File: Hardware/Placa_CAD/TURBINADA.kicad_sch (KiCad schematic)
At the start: 49 parts, among them J1 TURBINA, J2 RESISTENCIAS, J3 BATERIA, J4 ICSP, Q1 IXTP44P15T, Q2 IXTP36P15P, Q3 FQN1N50C, Q4 FQN1N50C, U1 PIC16F18324-xSL, U2 ADP2302ARDZ-5.0

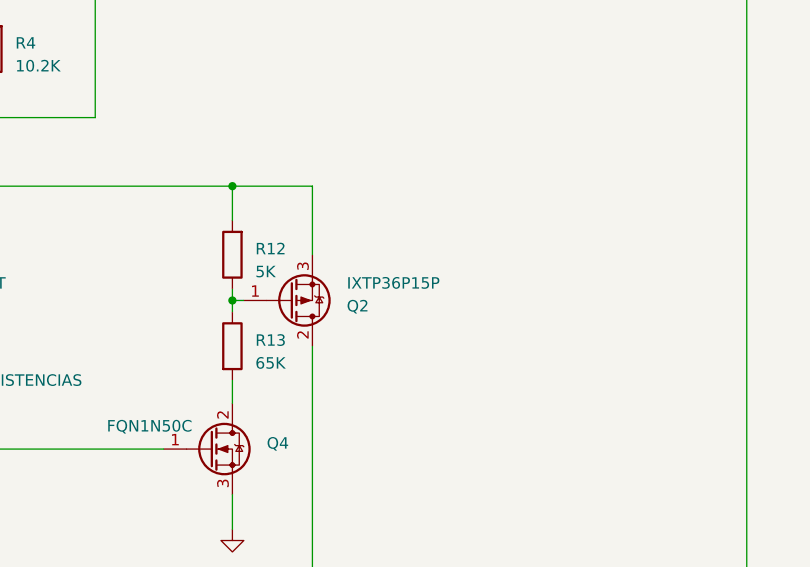
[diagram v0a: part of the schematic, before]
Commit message: Corrected some part numbers
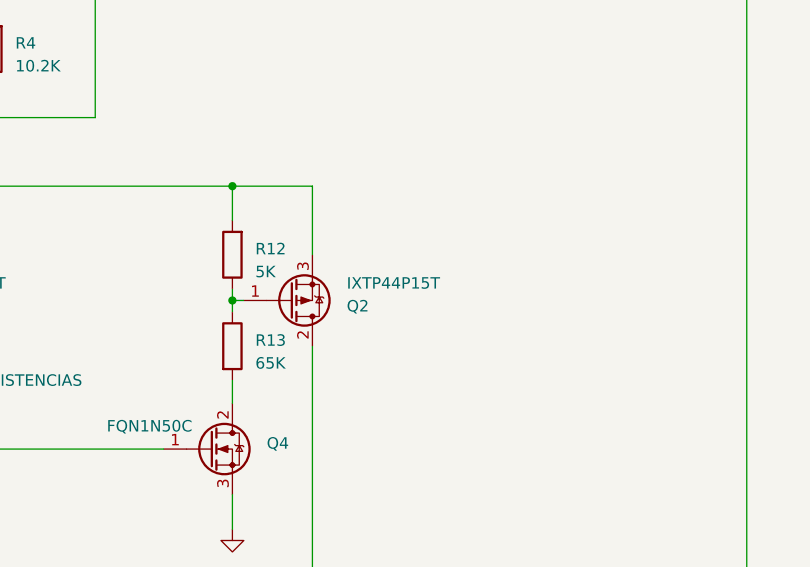
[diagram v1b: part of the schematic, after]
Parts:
- Q1: Part (none) -> IXTP44P15T
- Q2: value IXTP36P15P -> IXTP44P15T; Part (none) -> IXTP44P15T
- Q3, Q4: Part (none) -> FQN1N50C
- R14: Part CMF5510K000FKEK -> CMF5510K000FKEK
- R2: Part CMF5510K000FHEB -> CMF5510K000FKEK
- R3: Part CMF5510K000FKEK -> CMF5578K700FHEB
- R4: Part CMF5510K000FKEK -> CMF5510K200FHEB
- U1: Part (none) -> PIC16F18324
- U2: Part (none) -> ADP2302ARDZ-5.0
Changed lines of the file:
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@@
+      (effects (font (size 1.27 1.27)) hide)
+    )
+    (property "Part" "FQN1N50C" (at 212.09 90.17 0)
       (effects (font (size 1.27 1.27)) hide)
     )
@@
       (effects (font (size 1.27 1.27)) hide)
     )
-    (pin "2")
-    (pin "1")
+    (pin "1")
+    (pin "2")
     (instances
       (project "TURBINADA"
@@
       (effects (font (size 1.27 1.27)) hide)
     )
-    (property "Part" "CMF5510K000FKEK " (at 187.96 45.72 0)
+    (property "Part" "CMF5510K200FHEB" (at 187.96 45.72 0)
       (effects (font (size 1.27 1.27)) hide)
     )
@@
       (effects (font (size 1.27 1.27)) hide)
     )
-    (property "Part" "CMF5510K000FKEK" (at 238.76 125.73 0)
+    (property "Part" "CMF5510K000FKEK " (at 238.76 125.73 0)
       (effects (font (size 1.27 1.27)) hide)
     )
@@
       (effects (font (size 1.27 1.27)) hide)
     )
+    (property "Part" "FQN1N50C" (at 163.83 90.17 0)
+      (effects (font (size 1.27 1.27)) hide)
+    )
     (pin "1")
     (pin "2")
@@
       (effects (font (size 1.27 1.27)) hide)
     )
-    (property "Part" "CMF5510K000FHEB" (at 97.79 48.26 0)
+    (property "Part" "CMF5510K000FKEK " (at 97.79 48.26 0)
       (effects (font (size 1.27 1.27)) hide)
     )
@@
       (effects (font (size 1.27 1.27)) (justify left))
     )
-    (property "Value" "IXTP36P15P" (at 227.33 71.755 0)
+    (property "Value" "IXTP44P15T" (at 227.33 71.755 0)
       (effects (font (size 1.27 1.27)) (justify left))
     )
@@
       (effects (font (size 1.27 1.27)) hide)
     )
+    (property "Part" "IXTP44P15T" (at 220.98 73.66 0)
+      (effects (font (size 1.27 1.27)) hide)
+    )
     (pin "1")
     (pin "2")
@@
       (effects (font (size 1.27 1.27)) hide)
     )
-    (property "Part" "CMF5510K000FKEK " (at 187.96 35.56 0)
+    (property "Part" "CMF5578K700FHEB" (at 187.96 35.56 0)
       (effects (font (size 1.27 1.27)) hide)
     )
@@
     )
     (property "Datasheet" "~" (at 172.72 73.66 0)
+      (effects (font (size 1.27 1.27)) hide)
+    )
+    (property "Part" "IXTP44P15T" (at 172.72 73.66 0)
       (effects (font (size 1.27 1.27)) hide)
     )
@@
     )
     (property "Datasheet" "https://www.analog.com/media/en/technical-documentation/data-sheets/ADP2302_2303.pdf" (at 161.29 17.78 0)
+      (effects (font (size 1.27 1.27)) hide)
+    )
+    (property "Part" "ADP2302ARDZ-5.0" (at 156.21 33.02 0)
       (effects (font (size 1.27 1.27)) hide)
     )
@@
       (effects (font (size 1.27 1.27)) hide)
     )
+    (property "Part" "PIC16F18324" (at 114.3 97.79 0)
+      (effects (font (size 1.27 1.27)) hide)
+    )
